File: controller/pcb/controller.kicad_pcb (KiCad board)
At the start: 2 copper layers, 89.1 x 49.9 mm, 22 parts, among them SW1 SW_Push, SW2 SW_Push, SW3 SW_Push, SW4 SW_Push, U1 COM-09032, U2 COM-09032, U3 NRF24L01_Breakout, U4 ESP32C3-SUPERMINI, U5 74HC148

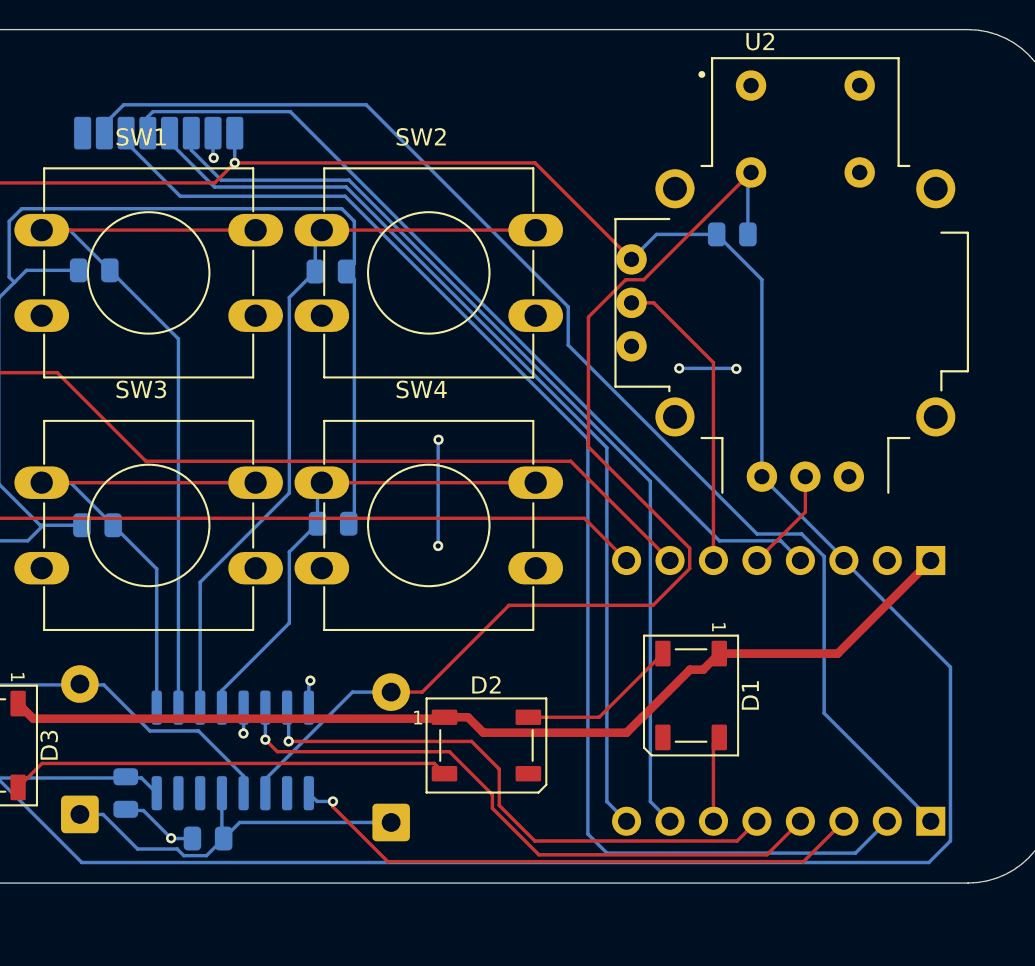
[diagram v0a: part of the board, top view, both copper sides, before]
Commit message: [firmware] add v202 protocl and nrf24 driver code
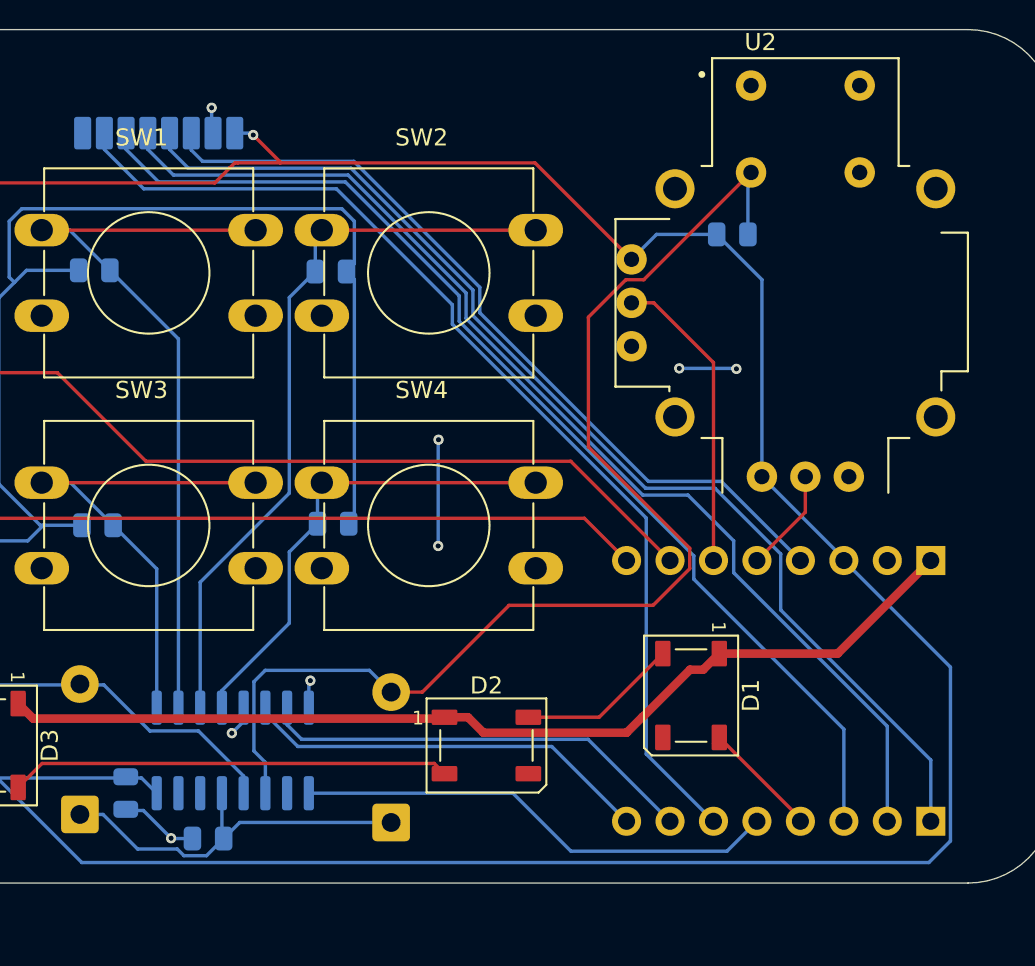
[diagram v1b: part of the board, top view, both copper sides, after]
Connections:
- U4 pad 1: MISO -> NRF_CS
- U4 pad 13: SCK -> NRF_CE
- U4 pad 2: MOSI -> SCK
- U4 pad 3: S0 -> MOSI
- U4 pad 4: S2 -> NEO
- U4 pad 5: S1 -> S0
- U4 pad 6: NEO -> MISO
- U4 pad 7: NRF_CE -> S1
- U4 pad 8: NRF_CS -> S2
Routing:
- net SCK: track 50.1 -> 65.7 mm
- net S2: track 37.2 -> 24.1 mm, vias 1 -> 0
- net MOSI: track 76.5 -> 64.0 mm
- net MISO: track 73.4 -> 61.6 mm
- net NRF_CS: track 55.8 -> 66.6 mm
- net NRF_CE: track 56.2 -> 47.4 mm
- net S1: track 33.5 -> 25.7 mm, vias 1 -> 0
- net S0: track 34.1 -> 28.3 mm, vias 1 -> 0
- net BTN_JOY_R: track 64.6 -> 69.9 mm
- net NEO: track 5.04 -> 7.34 mm
- net +3.3V: track 338.1 -> 339.8 mm

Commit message: [controller] add smoothing caps to ADC lines
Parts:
- added C2: 100nF, Capacitor_SMD:C_0805_2012Metric, F.Cu at (167.7, 85.0)
- added C3: 100nF, Capacitor_SMD:C_0805_2012Metric, F.Cu at (164.3, 85.0)
- added C4: 100nF, Capacitor_SMD:C_0805_2012Metric, F.Cu at (171.2, 85.0)
- added C5: 100nF, Capacitor_SMD:C_0805_2012Metric, F.Cu at (174.6, 85.0)
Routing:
- net JOY1_V: track 68.5 -> 71.1 mm
- net JOY2_H: track 6.07 -> 8.65 mm
- net JOY2_V: track 17.8 -> 20.3 mm
- net JOY1_H: track 52.4 -> 54.8 mm
- net BTN_JOY_R: track 69.9 -> 68.4 mm, vias 0 -> 1

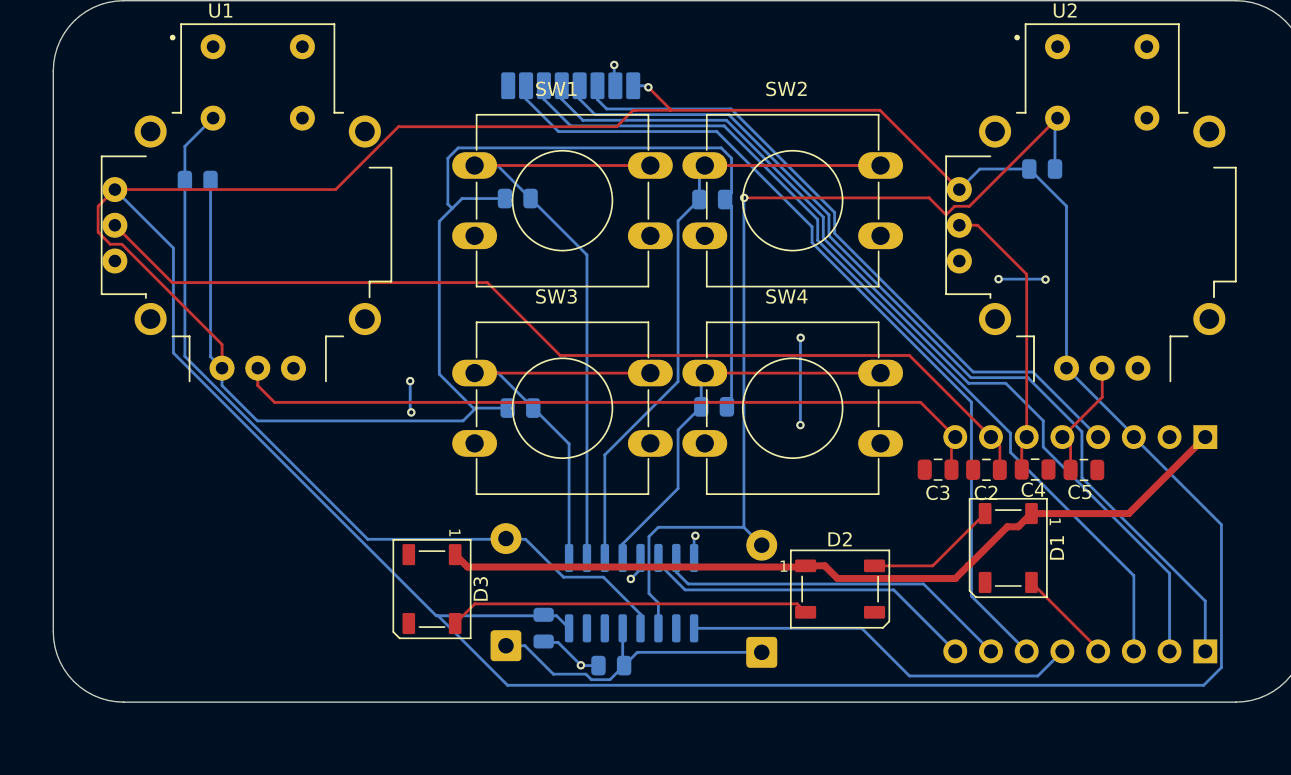
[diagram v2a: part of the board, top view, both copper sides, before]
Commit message: [controller] use higher quality external ADC
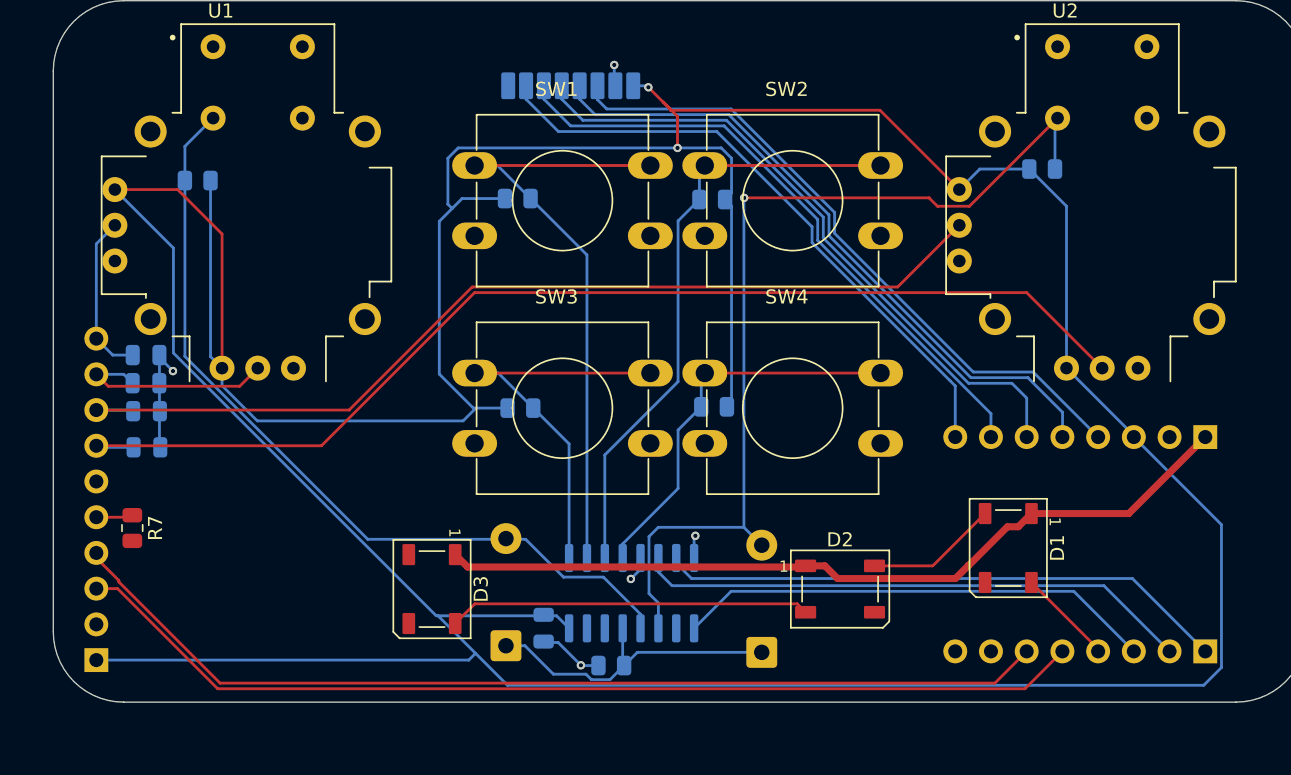
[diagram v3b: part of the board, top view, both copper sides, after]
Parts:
- added J1: Conn_01x10_Pin, Connector_PinHeader_2.54mm:PinHeader_1x10_P2.54mm_Vertical, B.Cu at (104.4, 98.5)
- added R7: 10k, Resistor_SMD:R_0805_2012Metric, F.Cu at (107.0, 89.1)
- C2, C3, C4, C5: moved to B.Cu
- moved C5 66.6 mm to (108.0, 83.4)
- moved C4 63.3 mm to (108.0, 80.8)
- moved C2 60.3 mm to (107.9, 76.8), turned to 0 degrees
- moved C3 56.7 mm to (107.9, 78.8), turned to 0 degrees
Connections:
- U4 pad 1: NRF_CS -> S1
- U4 pad 10: JOY1_V -> MOSI
- U4 pad 11: JOY2_V -> SCK
- U4 pad 12: JOY2_H -> NRF_CS
- U4 pad 2: SCK -> S2
- U4 pad 3: MOSI -> S0
- U4 pad 5: S0 -> SCL
- U4 pad 6: MISO -> SDA
- U4 pad 7: S1 -> unconnected-(U4-GPIO20-Pad7)
- U4 pad 8: S2 -> unconnected-(U4-GPIO21-Pad8)
- U4 pad 9: JOY1_H -> MISO
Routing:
- net SCL: track 0.00 -> 72.8 mm
- net JOY2_H: track 8.65 -> 81.0 mm
- net SDA: track 0.00 -> 71.2 mm
- net JOY1_V: track 71.1 -> 11.7 mm
- net JOY2_V: track 20.3 -> 69.5 mm
- net JOY1_H: track 54.8 -> 15.2 mm
- net MOSI: track 64.0 -> 44.5 mm
- net NRF_CS: track 66.6 -> 47.2 mm
- net SCK: track 65.7 -> 46.5 mm
- net MISO: track 61.6 -> 44.6 mm
- net S2: track 24.1 -> 39.7 mm
- net S1: track 25.7 -> 40.6 mm
- net +3.3V: track 339.8 -> 329.9 mm, vias 1 -> 2
- net S0: track 28.3 -> 34.1 mm
- net GND: track 21.4 -> 17.7 mm, vias 10 -> 5
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
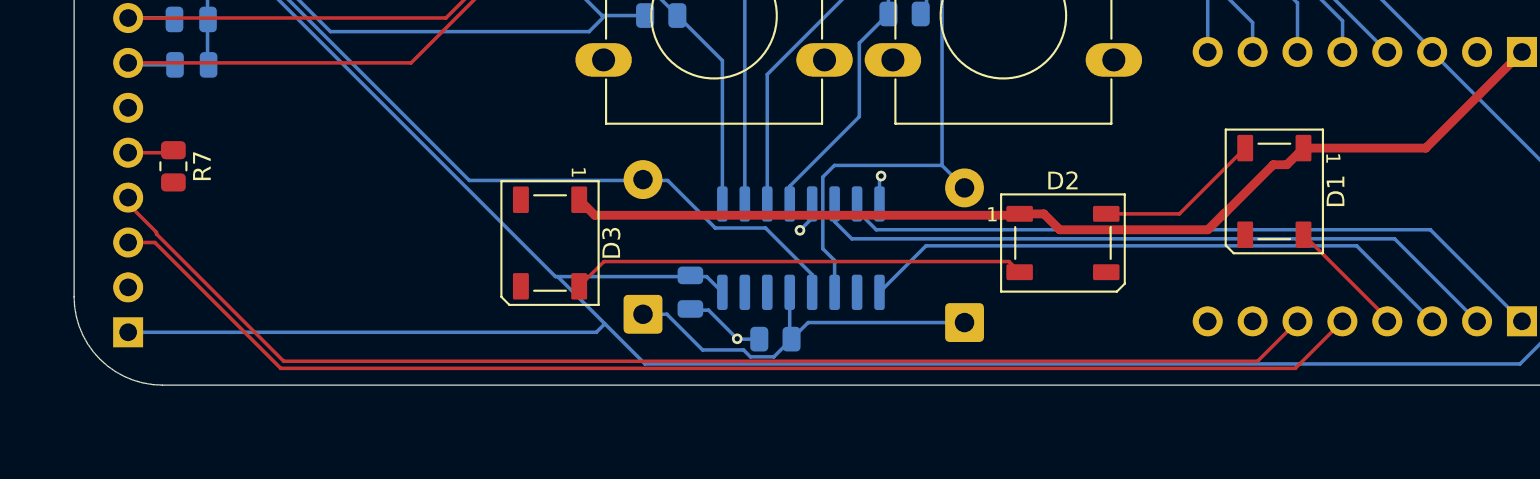
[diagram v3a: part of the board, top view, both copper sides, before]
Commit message: [controller] finish firmware, implement better ADC sampling w/ interrupt
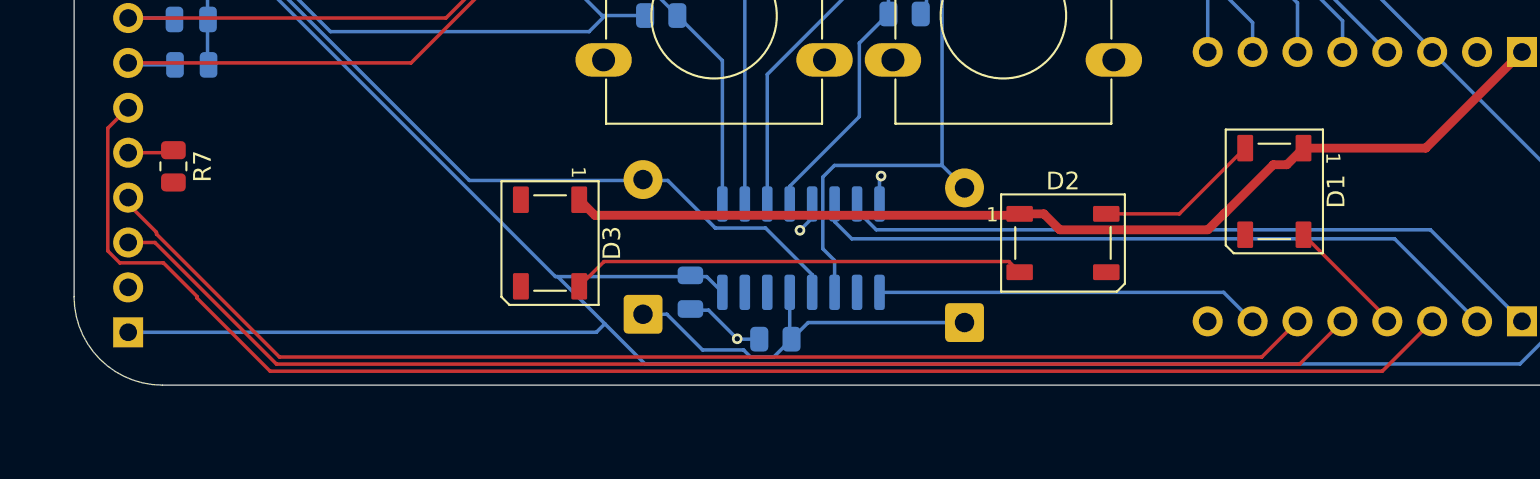
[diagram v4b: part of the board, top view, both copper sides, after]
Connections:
- J1 pad 6: unconnected-(J1-Pin_6-Pad6) -> ADC_INT
- U4 pad 3: S0 -> ADC_INT
- U4 pad 7: unconnected-(U4-GPIO20-Pad7) -> S0
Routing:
- net ADC_INT: track 0.00 -> 87.5 mm
- net S0: track 34.1 -> 21.8 mm
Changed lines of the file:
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@@
 	(net 38 "unconnected-(U3-IRQ-Pad8)")
 	(net 39 "Net-(J1-Pin_5)")
-	(net 40 "unconnected-(J1-Pin_6-Pad6)")
+	(net 40 "ADC_INT")
 	(net 41 "SDA")
 	(net 42 "SCL")
 	(net 43 "unconnected-(U4-GPIO21-Pad8)")
-	(net 44 "unconnected-(U4-GPIO20-Pad7)")
 	(footprint "Button_Switch_THT:SW_PUSH-12mm"
 		(layer "F.Cu")
@@
 			(layers "*.Cu" "*.Mask")
 			(remove_unused_layers no)
-			(net 40 "unconnected-(J1-Pin_6-Pad6)")
+			(net 40 "ADC_INT")
 			(pinfunction "Pin_6")
-			(pintype "passive+no_connect")
+			(pintype "passive")
 		)
 		(pad "7" thru_hole circle
@@
 			(layers "*.Cu" "*.Mask")
 			(remove_unused_layers no)
-			(net 25 "S0")
+			(net 40 "ADC_INT")
 			(pinfunction "GPIO7")
 			(pintype "unspecified")
@@
 			(layers "*.Cu" "*.Mask")
 			(remove_unused_layers no)
-			(net 44 "unconnected-(U4-GPIO20-Pad7)")
+			(net 25 "S0")
 			(pinfunction "GPIO20")
-			(pintype "unspecified+no_connect")
+			(pintype "unspecified")
 		)
 		(pad "8" thru_hole circle
@@
 	)
 	(segment
-		(start 146.91 96.25)
-		(end 149.539 93.621)
+		(start 166.38 96.25)
+		(end 168.02 97.89)
 		(width 0.2)
 		(layer "B.Cu")
@@
 	)
 	(segment
-		(start 173.911 93.621)
-		(end 178.18 97.89)
-		(width 0.2)
-		(layer "B.Cu")
-		(net 25)
-	)
-	(segment
-		(start 149.539 93.621)
-		(end 173.911 93.621)
+		(start 146.91 96.25)
+		(end 166.38 96.25)
 		(width 0.2)
 		(layer "B.Cu")
@@
 	)
 	(segment
-		(start 106.00324 92.95324)
-		(end 106.00324 92.85324)
+		(start 103.92324 94.581)
+		(end 103.249 93.90676)
 		(width 0.2)
 		(layer "F.Cu")
-		(net 41)
+		(net 40)
 	)
 	(segment
-		(start 168.301 100.149)
-		(end 113.199 100.149)
+		(start 106.391 94.581)
+		(end 103.92324 94.581)
+		(width 0.2)
+		(layer "F.Cu")
+		(net 40)
+	)
+	(segment
+		(start 108.3 96.49)
+		(end 106.391 94.581)
+		(width 0.2)
+		(layer "F.Cu")
+		(net 40)
+	)
+	(segment
+		(start 103.249 93.90676)
+		(end 103.249 86.961)
+		(width 0.2)
+		(layer "F.Cu")
+		(net 40)
+	)
+	(segment
+		(start 178.18 97.89)
+		(end 175.358 100.712)
+		(width 0.2)
+		(layer "F.Cu")
+		(net 40)
+	)
+	(segment
+		(start 108.3 96.58)
+		(end 108.3 96.49)
+		(width 0.2)
+		(layer "F.Cu")
+		(net 40)
+	)
+	(segment
+		(start 175.358 100.712)
+		(end 112.432 100.712)
+		(width 0.2)
+		(layer "F.Cu")
+		(net 40)
+	)
+	(segment
+		(start 103.249 86.961)
+		(end 104.4 85.81)
+		(width 0.2)
+		(layer "F.Cu")
+		(net 40)
+	)
+	(segment
+		(start 112.432 100.712)
+		(end 108.3 96.58)
+		(width 0.2)
+		(layer "F.Cu")
+		(net 40)
+	)
+	(segment
+		(start 168.54 99.91)
+		(end 112.96 99.91)
 		(width 0.2)
 		(layer "F.Cu")
@@
 	)
 	(segment
-		(start 106.00324 92.85324)
-		(end 104.4 91.25)
+		(start 106.00324 92.95324)
+		(end 106.00324 92.85324)
 		(width 0.2)
 		(layer "F.Cu")
@@
 	)
 	(segment
+		(start 106.00324 92.85324)
+		(end 104.4 91.25)
+		(width 0.2)
+		(layer "F.Cu")
+		(net 41)
+	)
+	(segment
 		(start 170.56 97.89)
-		(end 168.301 100.149)
+		(end 168.54 99.91)
 		(width 0.2)
 		(layer "F.Cu")
@@
 	)
 	(segment
-		(start 113.199 100.149)
+		(start 112.96 99.91)
 		(end 106.00324 92.95324)
 		(width 0.2)
@@
 	)
 	(segment
-		(start 104.4 93.43)
-		(end 105.9129 93.43)
+		(start 112.7939 100.311)
+		(end 170.679 100.311)
 		(width 0.2)
 		(layer "F.Cu")
@@
 	)
 	(segment
-		(start 170.44 100.55)
-		(end 173.1 97.89)
+		(start 104.4 93.43)
+		(end 105.9129 93.43)
 		(width 0.2)
 		(layer "F.Cu")
@@
 	)
 	(segment
-		(start 113.0329 100.55)
-		(end 170.44 100.55)
+		(start 170.679 100.311)
+		(end 173.1 97.89)
 		(width 0.2)
 		(layer "F.Cu")
@@
 	(segment
 		(start 105.9129 93.43)
-		(end 113.0329 100.55)
+		(end 112.7939 100.311)
 		(width 0.2)
 		(layer "F.Cu")

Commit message: [bom] change battery and [controller] add button 3d files
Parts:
- SW1, SW2, SW3, SW4: footprint Button_Switch_THT:SW_PUSH-12mm -> stuff:SW_PUSH-12mm
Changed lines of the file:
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@@
 	(net 42 "SCL")
 	(net 43 "unconnected-(U4-GPIO21-Pad8)")
-	(footprint "Button_Switch_THT:SW_PUSH-12mm"
+	(footprint "stuff:SW_PUSH-12mm"
 		(layer "F.Cu")
 		(at 131.3 63.34)
@@
 			)
 		)
+		(model "${KIPRJMOD}/libraries/stuff.3dshapes/12mm-button.step"
+			(offset
+				(xyz 6.4 -2.4 0.3)
+			)
+			(scale
+				(xyz 1 1 1)
+			)
+			(rotate
+				(xyz -90 -0 -0)
+			)
+		)
 	)
-	(footprint "Button_Switch_THT:SW_PUSH-12mm"
+	(footprint "stuff:SW_PUSH-12mm"
 		(layer "F.Cu")
 		(at 147.67 78.1)
@@
 			)
 		)
+		(model "${KIPRJMOD}/libraries/stuff.3dshapes/12mm-button.step"
+			(offset
+				(xyz 6.4 -2.4 0.3)
+			)
+			(scale
+				(xyz 1 1 1)
+			)
+			(rotate
+				(xyz -90 -0 -0)
+			)
+		)
 	)
 	(footprint "LED_SMD:LED_WS2812B_PLCC4_5.0x5.0mm_P3.2mm"
@@
 		)
 	)
-	(footprint "Button_Switch_THT:SW_PUSH-12mm"
+	(footprint "stuff:SW_PUSH-12mm"
 		(layer "F.Cu")
 		(at 147.67 63.34)
@@
 			)
 		)
+		(model "${KIPRJMOD}/libraries/stuff.3dshapes/12mm-button.step"
+			(offset
+				(xyz 6.4 -2.4 0.3)
+			)
+			(scale
+				(xyz 1 1 1)
+			)
+			(rotate
+				(xyz -90 -0 -0)
+			)
+		)
 	)
 	(footprint "Resistor_SMD:R_0805_2012Metric"
@@
 		)
 	)
-	(footprint "Button_Switch_THT:SW_PUSH-12mm"
+	(footprint "stuff:SW_PUSH-12mm"
 		(layer "F.Cu")
 		(at 131.3 78.1)
@@
 			)
 		)
+		(model "${KIPRJMOD}/libraries/stuff.3dshapes/12mm-button.step"
+			(offset
+				(xyz 6.4 -2.4 0.3)
+			)
+			(scale
+				(xyz 1 1 1)
+			)
+			(rotate
+				(xyz -90 -0 -0)
+			)
+		)
